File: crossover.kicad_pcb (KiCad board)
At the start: 2 copper layers, 58 x 29 mm, 18 parts, among them J1 Connector, U7 LF356, U8 LF356

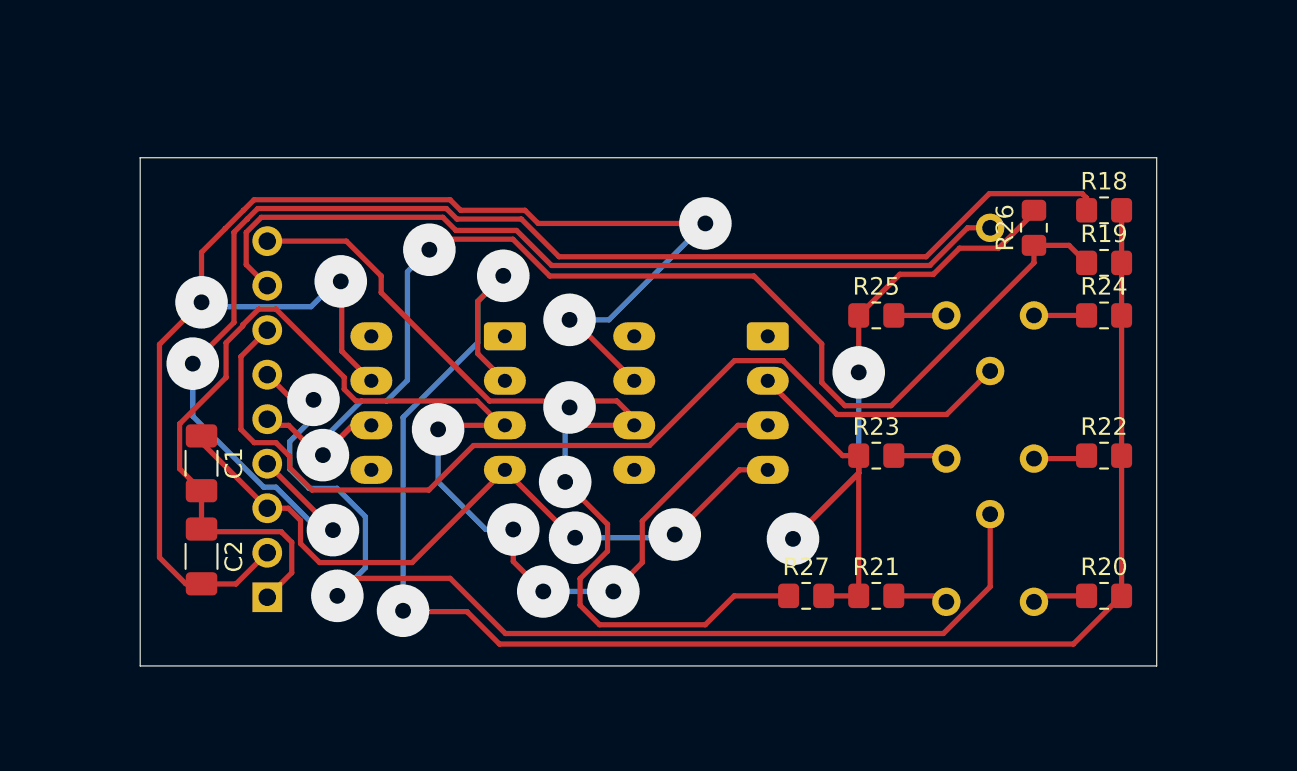
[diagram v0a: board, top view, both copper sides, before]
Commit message: Added JST
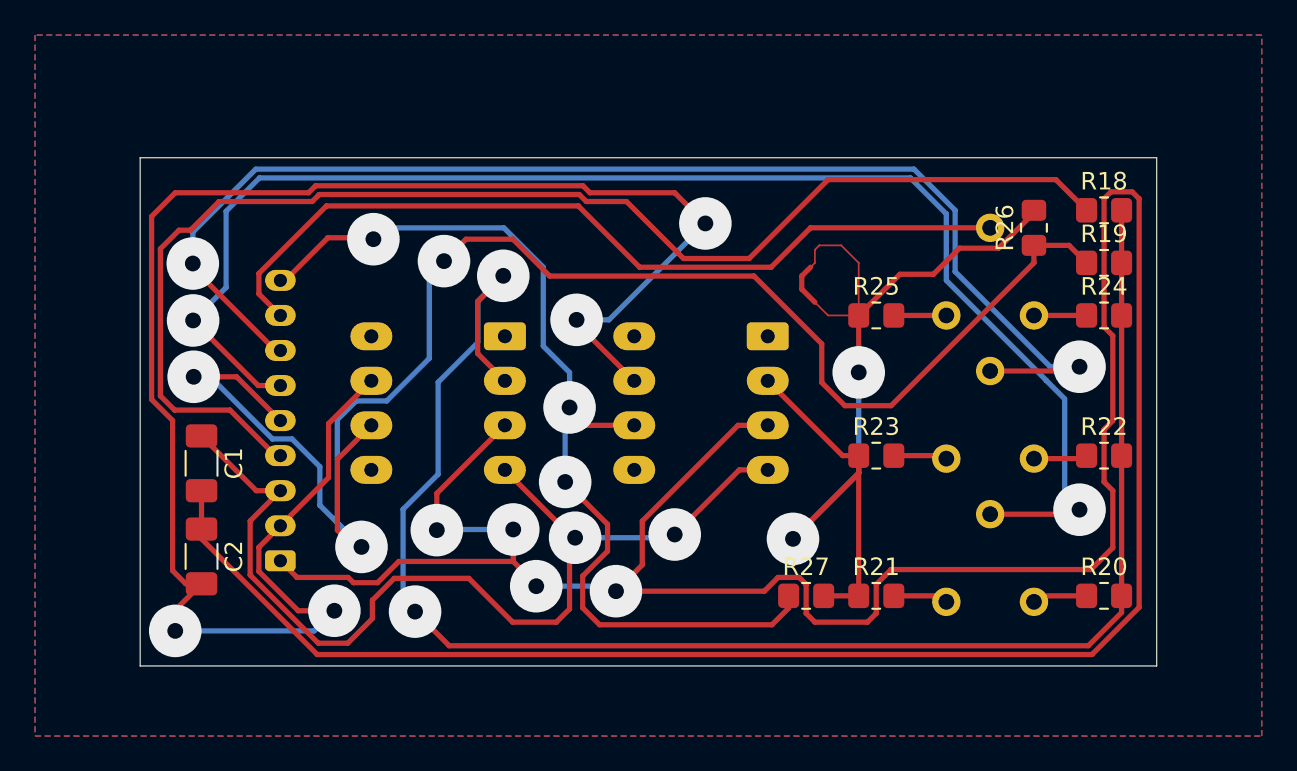
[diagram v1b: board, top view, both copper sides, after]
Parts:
- J1: footprint Connector_PinHeader_2.54mm:PinHeader_1x09_P2.54mm_Vertical -> Connector_JST:JST_PH_B9B-PH-K_1x09_P2.00mm_Vertical
- moved J1 2.21 mm to (104.0, 85.0), turned to 90 degrees
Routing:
- net GND: track 75.6 -> 188.5 mm
- net BF_In: track 72.6 -> 97.1 mm, vias 2 -> 3
- net High: track 62.6 -> 81.5 mm
- net Mid: track 56.2 -> 72.7 mm, vias 0 -> 2
- net -5v: track 41.3 -> 57.1 mm
- net +5v: track 86.7 -> 102.0 mm
- net Net-(U8--): track 50.0 -> 62.4 mm
- net Vin: track 80.2 -> 74.6 mm, vias 2 -> 0
- net Vout: track 55.9 -> 56.1 mm, vias 2 -> 3
- added copper zone on B.Cu, net GND
- added copper zone on F.Cu, net GND
